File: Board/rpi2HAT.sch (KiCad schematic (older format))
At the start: 76 parts, among them J1 FJ, J2 FJ, J3 FJ, J4 FJ, J5 FJ, J6 FJ, P1 CONN_01X03, P10 CONN_01X03, P11 CONN_01X03, P12 CONN_01X03, P13 CONN_01X03, P14 CONN_01X03, P15 CONN_01X03, P16 CONN_01X03, P2 CONN_01X03, P3 CONN_01X03, P4 CONN_01X03, P5 CONN_01X03, P6 CONN_01X03, P7 CONN_01X03, P8 CONN_01X03, P9 CONN_01X03, U1 BMP180-barometr, U2 7805

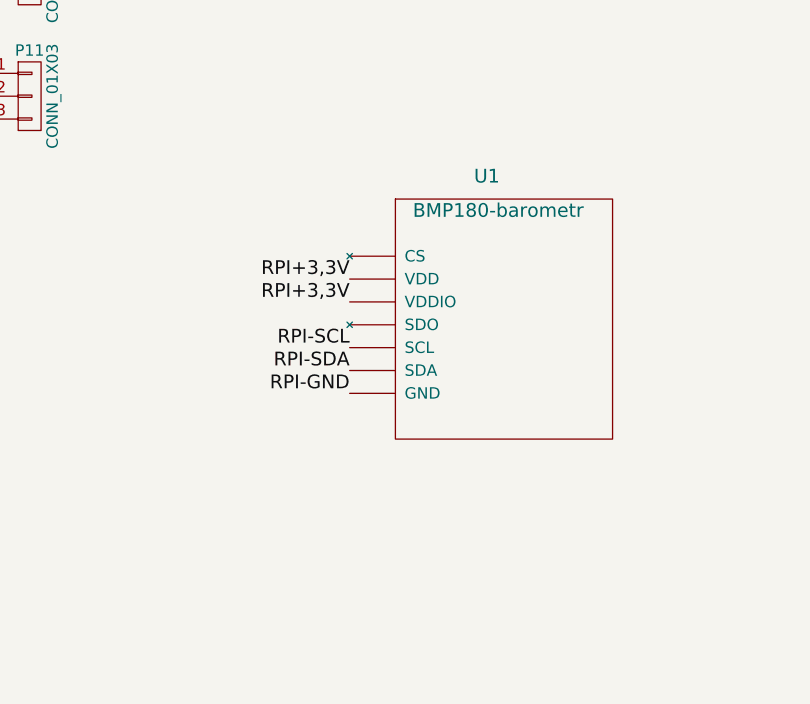
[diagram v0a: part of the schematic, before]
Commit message: Corrected some footprints.
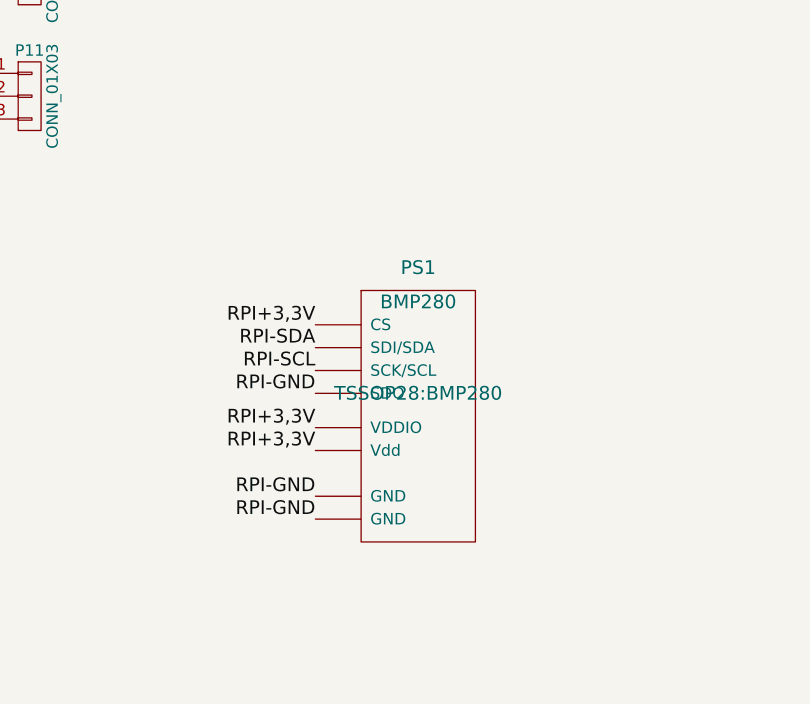
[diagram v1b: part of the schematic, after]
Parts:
- removed U1: BMP180-barometr, TSSOP28:BMP180, symbol BMP180-barometr
- added PS1: BMP280, TSSOP28:BMP280, symbol BMP280
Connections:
- net GND-SERVO: now also PS1.1 (GND), PS1.5 (SDO), PS1.7 (GND)
- net RPI+3,3V: now also PS1.2 (CS), PS1.6 (VDDIO), PS1.8 (Vdd)
- net RPI-SCL: now also PS1.4 (SCK/SCL)
- net RPI-SDA: now also PS1.3 (SDI/SDA)
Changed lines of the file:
@@
 RPI-GND
-$Comp
-L BMP180-barometr U1
-U 1 1 56AD7F4C
-P 3400 7050
-F 0 "U1" H 3350 7600 60  0000 C CNN
-F 1 "BMP180-barometr" H 3400 7450 60  0000 C CNN
-F 2 "TSSOP28:BMP180" H 3300 6300 60  0001 C CNN
-F 3 "" H 3300 6300 60  0000 C CNN
-	1    3400 7050
-	1    0    0    -1
-$EndComp
 $Comp
 L MCP3021 ADC1
@@
 Text Label 2650 9950 2    60   ~ 0
 RPI-SCL
-Text Label 2750 7250 2    60   ~ 0
-RPI-SCL
 Text Label 4900 3950 2    60   ~ 0
 RPI-SDA
@@
 Text Label 2650 9800 2    60   ~ 0
 RPI-SDA
-Text Label 2750 7350 2    60   ~ 0
-RPI-SDA
-Text Label 2750 6950 2    60   ~ 0
-RPI+3,3V
-Text Label 2750 7050 2    60   ~ 0
-RPI+3,3V
-Text Label 2750 7450 2    60   ~ 0
-RPI-GND
 $Comp
 L FJ J4
@@
 Text Label 6700 9050 2    60   ~ 0
 +5-SERVO
+$Comp
+L BMP280 PS1
+U 1 1 56D32CEA
+P 3050 7450
+F 0 "PS1" H 3050 8000 60  0000 C CNN
+F 1 "BMP280" H 3050 7850 60  0000 C CNN
+F 2 "TSSOP28:BMP280" H 3050 7450 60  0000 C CNN
+F 3 "" H 3050 7450 60  0000 C CNN
+	1    3050 7450
+	1    0    0    -1
+$EndComp
+Text Label 2600 7600 2    60   ~ 0
+RPI+3,3V
+Text Label 2600 7700 2    60   ~ 0
+RPI+3,3V
+Text Label 2600 7900 2    60   ~ 0
+RPI-GND
+Text Label 2600 8000 2    60   ~ 0
+RPI-GND
+Text Label 2600 7350 2    60   ~ 0
+RPI-SCL
+Text Label 2600 7250 2    60   ~ 0
+RPI-SDA
+Text Label 2600 7450 2    60   ~ 0
+RPI-GND
+Text Label 2600 7150 2    60   ~ 0
+RPI+3,3V
 $EndSCHEMATC

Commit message: Nowa wersja - rpi zero +, tylko 2 warstwy!
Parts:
- removed 5vin1: CONN_01X02, Pin_Headers:Pin_Header_Straight_1x02, symbol CONN_01X02
- removed C1, C2: CP, Capacitors_ThroughHole:C_Radial_D6.3_L11.2_P2.5, symbol CP
- removed C6, C9: CP, Capacitors_SMD:C_1206, symbol CP
- removed C7: C, Capacitors_SMD:C_1206, symbol C
- removed J1, J2: FJ, TSSOP28:FIXED_JUMPER, symbol FJ
- removed R3, R4: R, Resistors_SMD:R_1206, symbol R
- removed U2: 7805, TSSOP28:DPAK, symbol 7805
- added 5out1: CONN_01X02, Pin_Headers:Pin_Header_Straight_1x02, symbol CONN_01X02
- added C1, C6, C9: 100n, Capacitors_SMD:C_0603_HandSoldering, symbol C
- added C13, C14, C15, C16, C17, C18, C19, C20, C22, C23: 10u, Capacitors_SMD:C_0805, symbol C
- added C21: 100n, c2, symbol C
- added D2: D, Diodes_SMD:SOD-123, symbol D
- added L1: 1uH, Inductors_NEOSID:Neosid_Inductor_SM-NE30_SMD1210, symbol INDUCTOR
- added U1: TPS663061, TSSOP28:TPS6306, symbol TPS663061
- added U2: LD1117, Housings_SOIC:SOIC-8_3.9x4.9mm_Pitch1.27mm, symbol LD1117
- C10, C8: value C -> 100n; footprint Capacitors_SMD:C_1206 -> Capacitors_SMD:C_0603_HandSoldering
- C11, C12, C5: footprint Capacitors_SMD:C_1206 -> Capacitors_SMD:C_0805
- C3: value 10n -> 100n
- R1, R10, R11, R12, R13, R14, R15, R16, R17, R18, R19, R2, R20, R21, R22, R23, R24, R25, R26, R27, R28, R5, R6, R7, R8, R9: footprint Resistors_SMD:R_1206 -> Resistors_SMD:R_0805
- renumbered 5-15out1 to 5-15in1
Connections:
- net +5-SERVO: now also C10.2, 5out1.1 (P1), C16.1, C17.1, C18.1, C19.1, C20.1, C23.1, C9.2, U1.8 (FB), U1.9 (VOUT), U2.4 (Vin); no longer C8.1
- net EXT+: now also D2.2 (A)
- net GND-SERVO: now also C10.1, C8.1, IMU1.2 (A1), IMU1.3 (A2), 5out1.2 (P2), C1.1, C13.2, C14.2, C15.2, C16.2, C17.2, C18.2, C19.2, C20.2, C22.2, C23.2, C6.1, C9.1, U1.0 (PAD), U1.4 (PS/SYNC), U1.7 (GND), U2.1 (GND); no longer C10.2, C3.1, C4.1, C8.2
- net RPI+3,3V: now also C22.1, C6.2, U2.2 (Vout), U2.3 (Vout), U2.6 (Vout), U2.7 (Vout); no longer C10.1, C4.2, H1.1 (3.3V), IMU2.1 (RESV(VDD)), IMU2.8 (VDD), PS1.8 (Vdd)
- net at ADC1.3 (AIN), R1.2, R2.1: now also C1.2
- new net: C21.2, IMU2.1 (RESV(VDD))
- new net: C4.2, IMU2.8 (VDD)
- new net: C21.1, C3.1, C4.1
- new net: C8.2, PS1.8 (Vdd)
- new net: L1.1, U1.1 (L1)
- new net: L1.2, U1.10 (L2)
- new net: C13.1, C14.1, D2.1 (K), U1.2 (VIN), U1.3 (EN)
- new net: C15.1, U1.6 (VAUX)
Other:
- moved on the sheet: 5-15in1, C3, C4

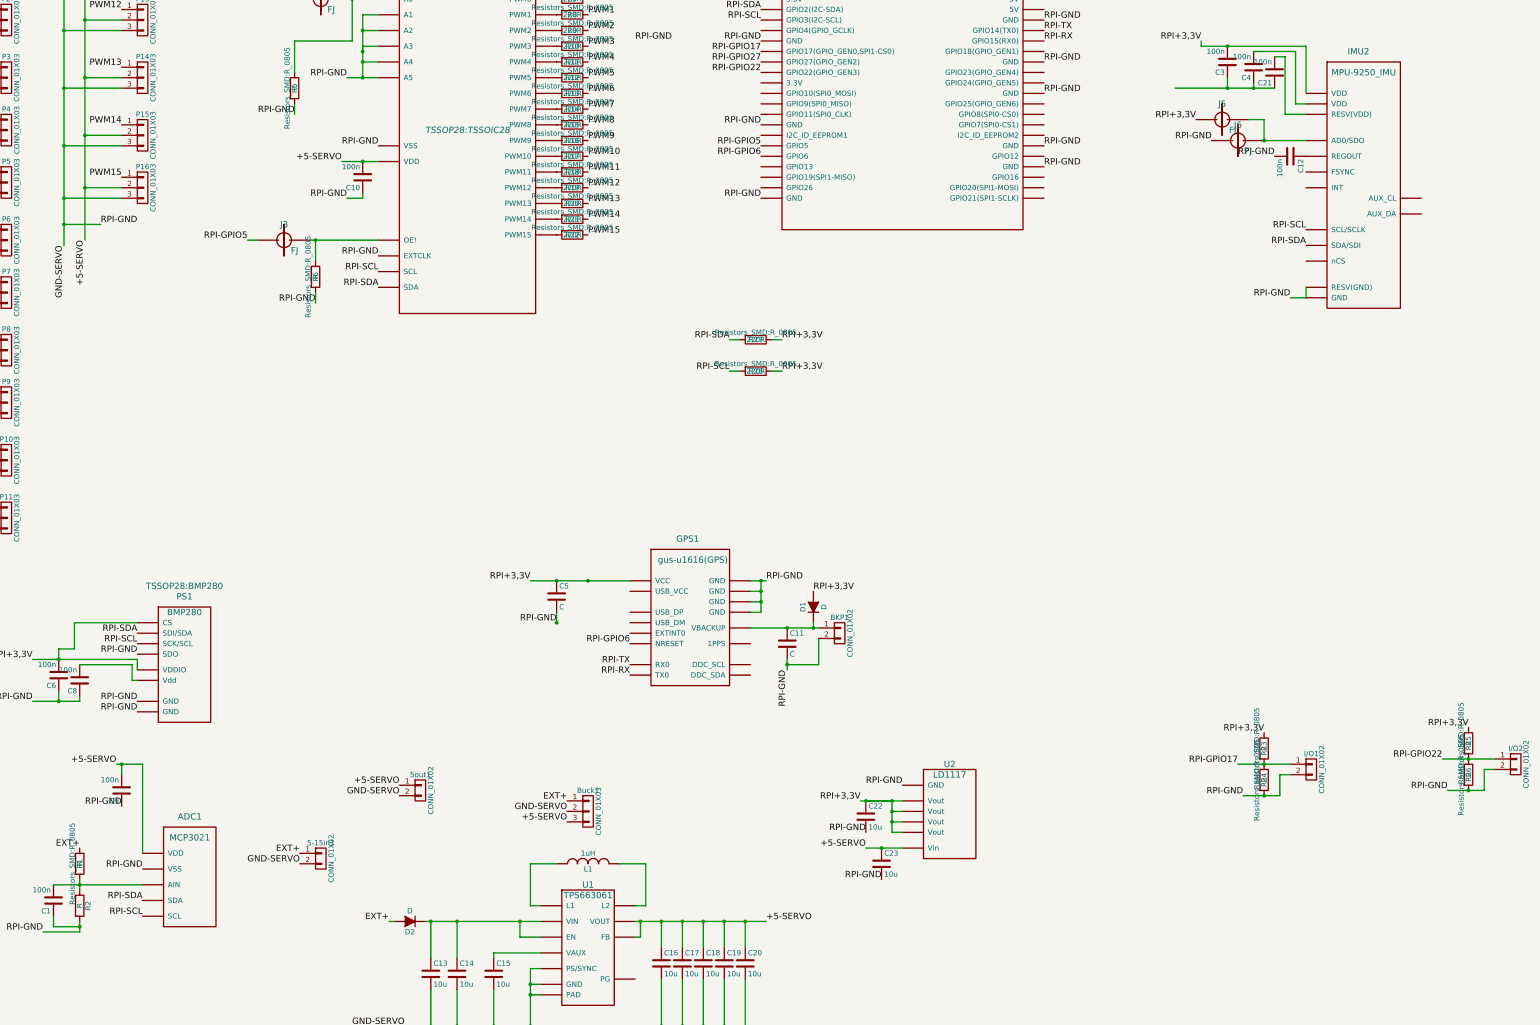
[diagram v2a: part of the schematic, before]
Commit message: added all components values on sch.
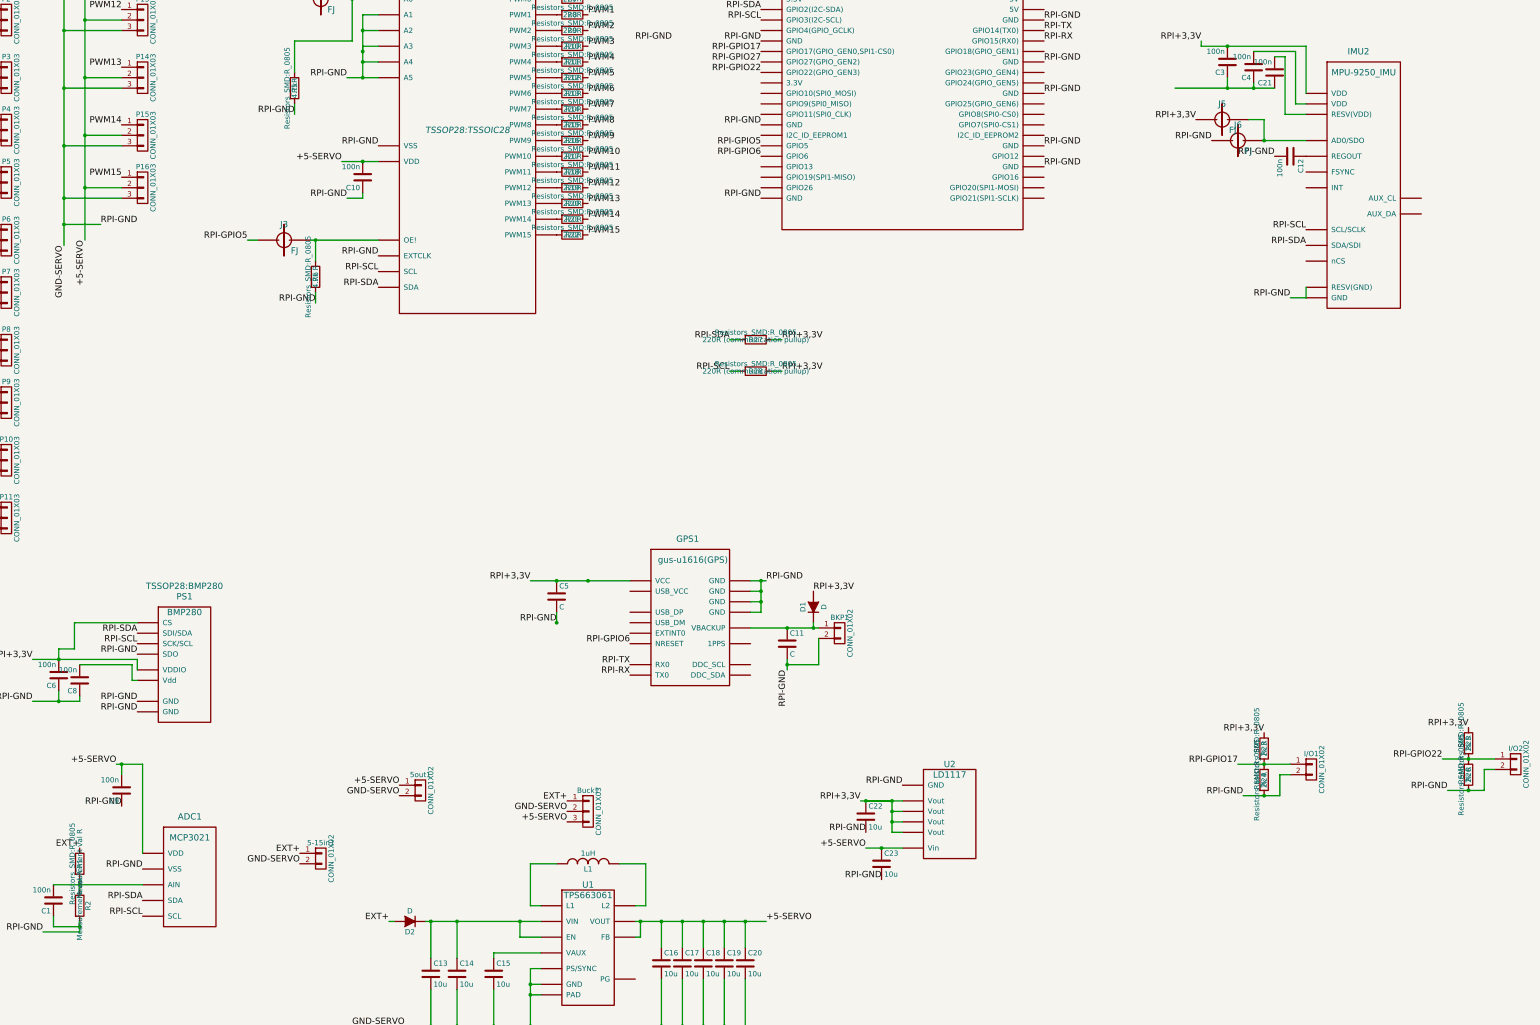
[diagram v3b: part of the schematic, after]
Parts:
- R1, R2: value R -> Measurement val R
- R23, R24, R25, R26: value R -> 2k R
- R27, R28: value 220R -> 220R (communication pullup)
- R5: value R -> 4.7kR
- R6: value R -> 4.7k R
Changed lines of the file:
@@
 P 2050 9450
 F 0 "R1" V 2050 9450 50  0000 C CNN
-F 1 "R" V 2050 9450 50  0000 C CNN
+F 1 "Measurement val R" V 2050 9450 50  0000 C CNN
 F 2 "Resistors_SMD:R_0805" V 1980 9450 50  0000 C CNN
 F 3 "" H 2050 9450 50  0000 C CNN
@@
 P 2050 9850
 F 0 "R2" V 2130 9850 50  0000 C CNN
-F 1 "R" V 2050 9850 50  0000 C CNN
+F 1 "Measurement val R" V 2050 9850 50  0000 C CNN
 F 2 "Resistors_SMD:R_0805" V 1980 9850 50  0001 C CNN
 F 3 "" H 2050 9850 50  0000 C CNN
@@
 P 4100 2050
 F 0 "R5" V 4100 2050 50  0000 C CNN
-F 1 "R" V 4100 2050 50  0000 C CNN
+F 1 "4.7kR" V 4100 2050 50  0000 C CNN
 F 2 "Resistors_SMD:R_0805" V 4030 2050 50  0000 C CNN
 F 3 "" H 4100 2050 50  0000 C CNN
@@
 P 4300 3850
 F 0 "R6" V 4300 3850 50  0000 C CNN
-F 1 "R" V 4300 3850 50  0000 C CNN
+F 1 "4.7k R" V 4300 3850 50  0000 C CNN
 F 2 "Resistors_SMD:R_0805" V 4230 3850 50  0000 C CNN
 F 3 "" H 4300 3850 50  0000 C CNN
@@
 P 15300 8300
 F 0 "R25" V 15300 8300 50  0000 C CNN
-F 1 "R" V 15300 8300 50  0000 C CNN
+F 1 "2k R" V 15300 8300 50  0000 C CNN
 F 2 "Resistors_SMD:R_0805" V 15230 8300 50  0000 C CNN
 F 3 "" H 15300 8300 50  0000 C CNN
@@
 P 15300 8600
 F 0 "R26" V 15300 8600 50  0000 C CNN
-F 1 "R" V 15300 8600 50  0000 C CNN
+F 1 "2k R" V 15300 8600 50  0000 C CNN
 F 2 "Resistors_SMD:R_0805" V 15230 8600 50  0000 C CNN
 F 3 "" H 15300 8600 50  0000 C CNN
@@
 P 13350 8350
 F 0 "R23" V 13350 8350 50  0000 C CNN
-F 1 "R" V 13350 8350 50  0000 C CNN
+F 1 "2k R" V 13350 8350 50  0000 C CNN
 F 2 "Resistors_SMD:R_0805" V 13280 8350 50  0000 C CNN
 F 3 "" H 13350 8350 50  0000 C CNN
@@
 P 13350 8650
 F 0 "R24" V 13350 8650 50  0000 C CNN
-F 1 "R" V 13350 8650 50  0000 C CNN
+F 1 "2k R" V 13350 8650 50  0000 C CNN
 F 2 "Resistors_SMD:R_0805" V 13280 8650 50  0000 C CNN
 F 3 "" H 13350 8650 50  0000 C CNN
@@
 P 8500 4450
 F 0 "R27" V 8500 4450 50  0000 C CNN
-F 1 "220R" V 8500 4450 50  0000 C CNN
+F 1 "220R (communication pullup)" V 8500 4450 50  0000 C CNN
 F 2 "Resistors_SMD:R_0805" V 8430 4450 50  0000 C CNN
 F 3 "" H 8500 4450 50  0000 C CNN
@@
 P 8500 4750
 F 0 "R28" V 8500 4750 50  0000 C CNN
-F 1 "220R" V 8500 4750 50  0000 C CNN
+F 1 "220R (communication pullup)" V 8500 4750 50  0000 C CNN
 F 2 "Resistors_SMD:R_0805" V 8430 4750 50  0000 C CNN
 F 3 "" H 8500 4750 50  0000 C CNN
